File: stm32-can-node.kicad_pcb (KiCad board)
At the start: 4 copper layers, 40 x 25 mm, 41 parts, among them J1 Conn_01x04_Pin, J2 Conn_01x10_Pin, J3 Conn_01x10_Pin, J4 Conn_01x05_Pin, U1 DS2484R_T, U2 R-783.3-0.5, U3 STM32U535CETx, U4 SN65HVD234, Y1 16MHz

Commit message: better pcb layout
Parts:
- added C16: 100n, Capacitor_SMD:C_0402_1005Metric, F.Cu at (91.2, 53.5)
- moved C15 2.16 mm to (78.9, 63.7)
- moved C3 1.68 mm to (79.6, 65.2), turned to 0 degrees
- moved C6 1.56 mm to (76.1, 64.8), turned to -90 degrees
- moved R2 1.30 mm to (67.8, 54.5)
- moved C7 1.30 mm to (69.4, 54.1), turned to 0 degrees
- moved C14 0.58 mm to (78.4, 60.4)
- moved R6 0.35 mm to (86.4, 51.4)
- moved U1 0.30 mm to (88.6, 53.5)
- moved C4 0.26 mm to (66.4, 57.1), turned to -90 degrees
- moved C1 0.25 mm to (97.6, 65.7), turned to 0 degrees
- moved C2 0.20 mm to (84.5, 64.8), turned to 180 degrees
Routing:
- net +3.3V: track 22.8 -> 33.5 mm, vias 14 -> 15
- net CANH: track 20.3 -> 16.4 mm, vias 1 -> 2
- net CANL: track 20.2 -> 16.6 mm, vias 1 -> 2
- net Net-(U3-VCAP): track 3.47 -> 5.52 mm
- net GND: track 34.7 -> 36.5 mm, vias 25 -> 24
- net CAN_RX: track 4.86 -> 6.55 mm
- net +VIN: track 9.15 -> 7.85 mm
- net BOOT0: track 6.56 -> 5.74 mm, vias 2 -> 0

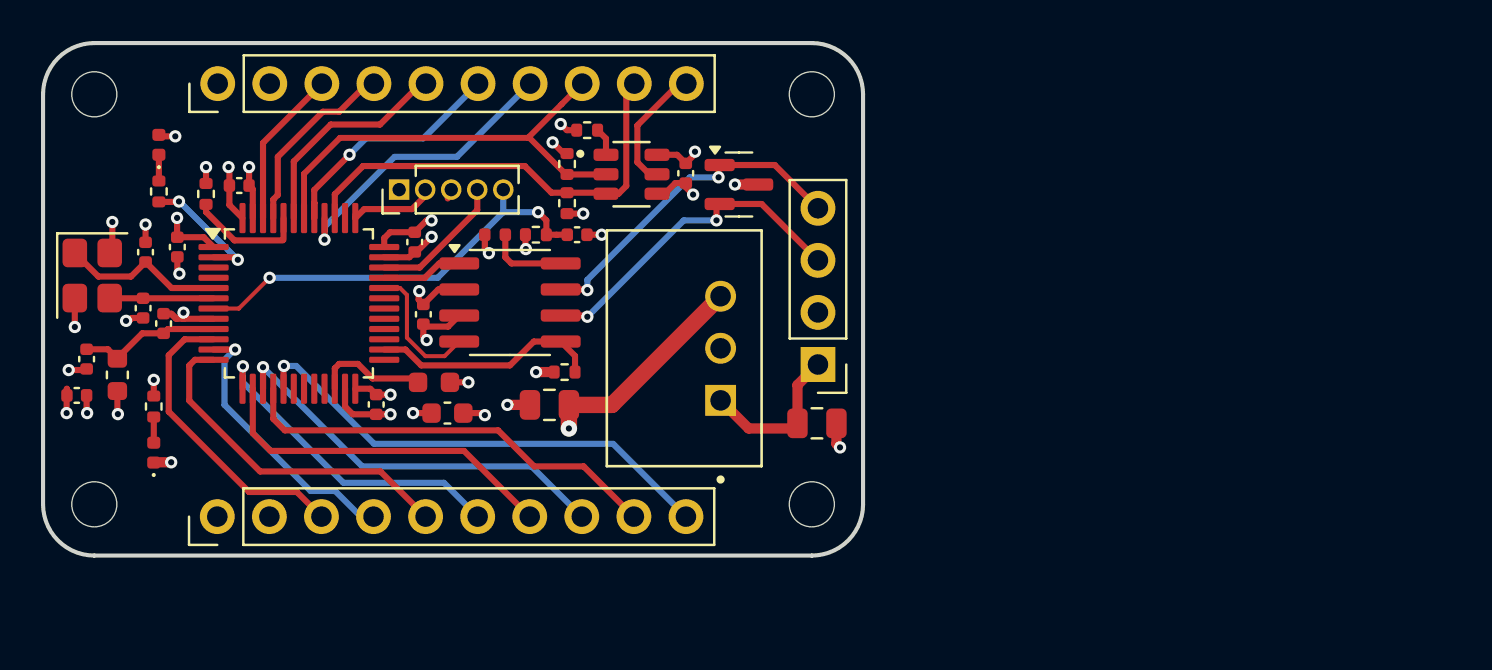
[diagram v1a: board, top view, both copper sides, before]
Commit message: change to 11-pin connectors
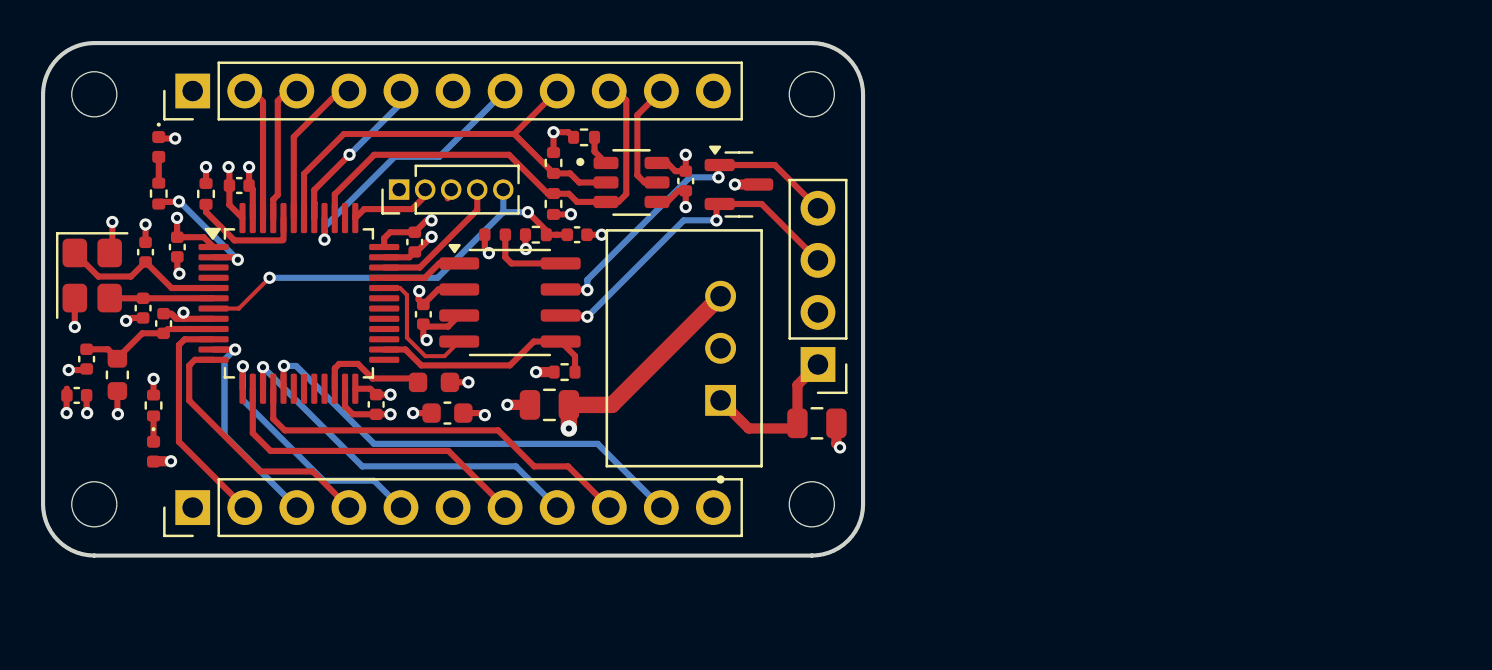
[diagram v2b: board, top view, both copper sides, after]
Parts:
- J2, J3: value Conn_01x10_Pin -> Conn_01x11_Pin; footprint Connector_PinHeader_2.54mm:PinHeader_1x10_P2.54mm_Vertical -> Connector_PinHeader_2.54mm:PinHeader_1x11_P2.54mm_Vertical
- moved J2 1.28 mm to (67.2, 69.8)
- moved J3 1.27 mm to (67.2, 49.5)
- moved R5 0.66 mm to (84.8, 53.0)
- moved R4 0.66 mm to (84.8, 55.0)
- moved U1 0.40 mm to (88.6, 54.0)
- moved R6 0.38 mm to (86.2, 51.8)
- moved C16 0.38 mm to (91.2, 53.9)
- moved D2 0.11 mm to (65.5, 52.2), turned to -90 degrees
- moved R9 0.11 mm to (65.5, 54.5)
- turned D1 to -90 degrees
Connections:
- D1 pad 1: +3.3V -> /PWR_LED_K
- D1 pad 2: /PWR_LED_K -> +3.3V
- D2 pad 1: Net-(D2-K) -> GND
- D2 pad 2: GND -> Net-(D2-A)
- J2 pad 2: GND -> PA0
- J2 pad 3: PA0 -> PA1
- J2 pad 4: PA1 -> PA2
- J2 pad 5: PA2 -> PA3
- J2 pad 6: PA3 -> GND
- J3 pad 2: GND -> PB9
- J3 pad 3: PB9 -> PB8
- J3 pad 4: PB8 -> PB7
- J3 pad 5: PB7 -> PB5
- J3 pad 6: PB5 -> GND
- R9 pad 2: Net-(D2-K) -> Net-(D2-A)
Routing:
- net PA2: track 16.9 -> 13.0 mm
- net PA0: track 14.8 -> 11.1 mm
- net PA3: track 16.1 -> 12.7 mm
- net PB7: track 11.0 -> 7.71 mm
- net PA1: track 13.5 -> 10.5 mm
- net PB8: track 9.25 -> 7.07 mm
- net PB4: track 14.6 -> 13.2 mm
- net PA6: track 21.0 -> 19.7 mm
- net PA5: track 19.6 -> 18.3 mm
- net PA4: track 17.4 -> 16.0 mm
- net PA7: track 23.8 -> 22.4 mm
- net Net-(D2-A): track 0.00 -> 1.28 mm
- net Net-(D2-K): track 1.28 -> 0.00 mm
- net I2C_SCL: track 22.2 -> 23.4 mm
- net PB9: track 8.05 -> 6.99 mm
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
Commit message: add step-down converter, update part values
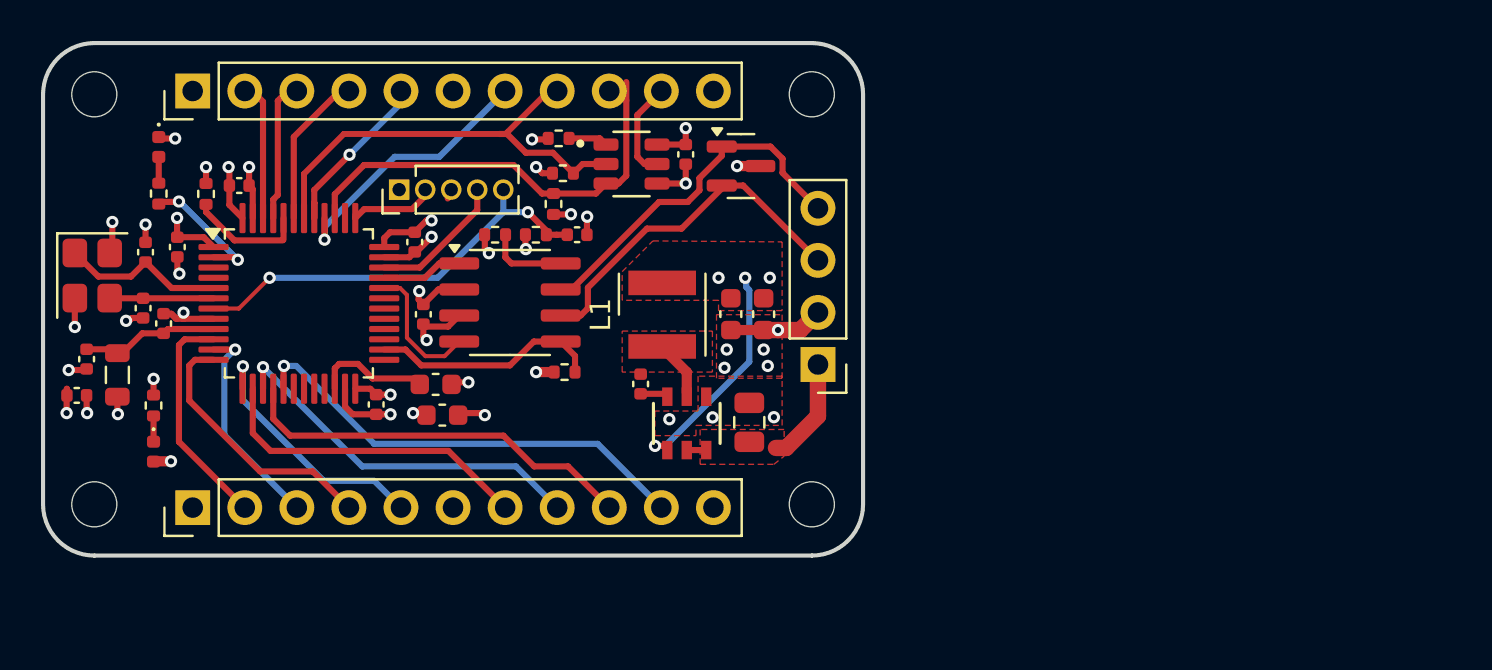
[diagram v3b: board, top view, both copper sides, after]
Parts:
- removed C2: 22u, Capacitor_SMD:C_0805_2012Metric
- removed U2: R-783.3-0.5, mrk:CONV_R-783.3-0.5
- added C18: 22uF, Capacitor_SMD:C_0603_1608Metric, F.Cu at (95.0, 60.4)
- added C19: 22uF, Capacitor_SMD:C_0603_1608Metric, F.Cu at (93.4, 60.4)
- added C20: 100nF, Capacitor_SMD:C_0402_1005Metric, F.Cu at (89.0, 63.8)
- added L1: 4.7uH, Inductor_SMD_Wurth:L_Wurth_WE-LQSH-4020, F.Cu at (90.0, 60.4)
- added U5: AP63203WU-7, footprints:AP63203WU-7_DIO, F.Cu at (91.2, 65.7)
- C1: value 22u -> 22uF
- C10, C11, C14, C16, C4, C5, C6, C7: value 100n -> 100nF
- C12, C13: value 10p -> 10pF
- C15: footprint PCM_JLCPCB:C_0603 -> Capacitor_SMD:C_0603_1608Metric
- C3: value 10u -> 10uF
- C8: value 10n -> 10nF
- C9: value 1u -> 1uF
- FB1: footprint Inductor_SMD:L_0603_1608Metric -> Inductor_SMD:L_0805_2012Metric
- R3: footprint PCM_JLCPCB:R_0402 -> Resistor_SMD:R_0402_1005Metric
- moved C1 3.30 mm to (94.3, 65.7), turned to 90 degrees
- moved C16 1.30 mm to (91.2, 52.6)
- moved R6 1.24 mm to (85.0, 51.8)
- moved D3 0.91 mm to (93.9, 53.1)
- moved U1 0.90 mm to (88.6, 53.1)
- moved R5 0.68 mm to (85.2, 53.5), turned to 0 degrees
- moved C3 0.27 mm to (79.3, 65.3)
- moved C15 0.13 mm to (79.0, 63.8)
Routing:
- net /SW: track 0.00 -> 3.05 mm
- net GND: track 35.9 -> 38.2 mm, vias 24 -> 30
- net +VIN: track 7.85 -> 6.16 mm
- net /BST: track 0.00 -> 1.45 mm
- net CANL: track 16.6 -> 17.8 mm, vias 2 -> 0
- net CANH: track 16.4 -> 17.4 mm, vias 2 -> 0
- net 1-W: track 5.70 -> 4.80 mm
- net I2C_SCL: track 23.4 -> 22.7 mm
- net +3.3V: track 33.8 -> 34.1 mm, vias 14 -> 18
- added copper zone on F.Cu, net +3.3V
- added copper zone on F.Cu, net +VIN
- added copper zone on F.Cu, net /SW
- added copper zone on F.Cu, net GND

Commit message: remove vias under mcu
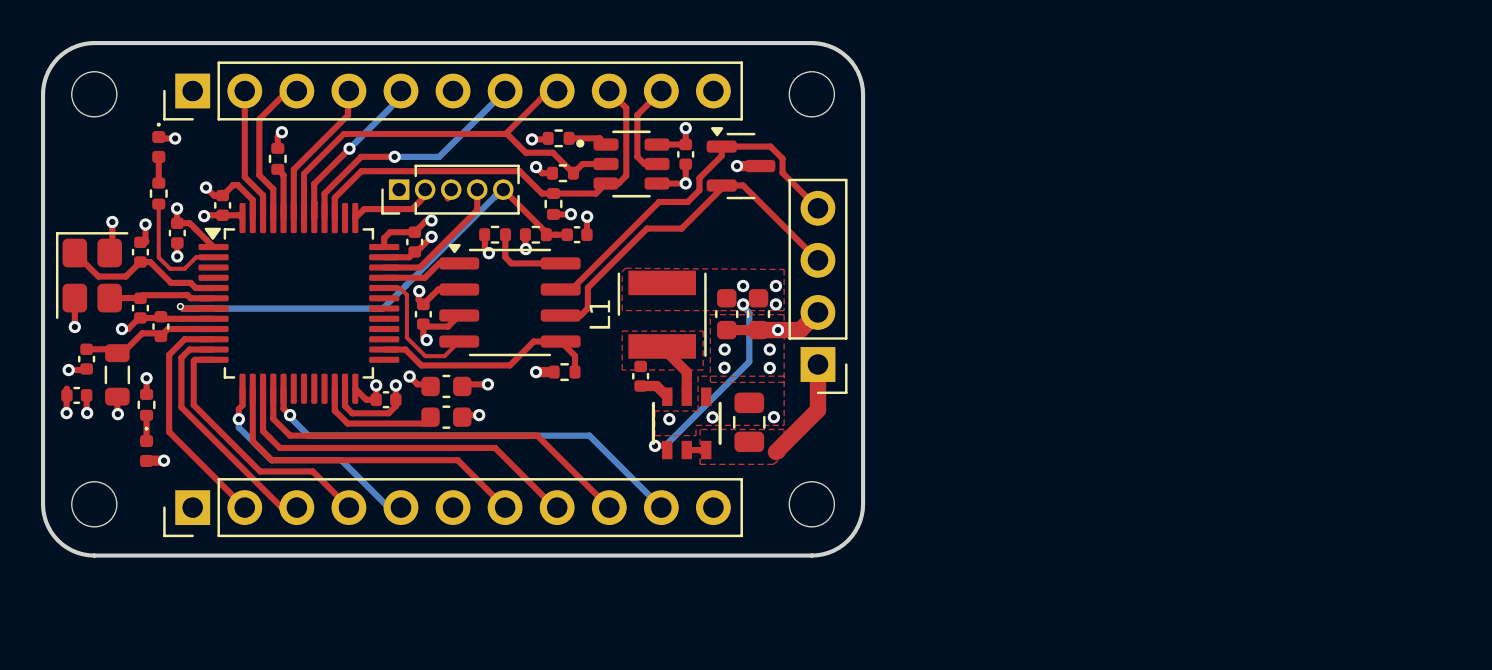
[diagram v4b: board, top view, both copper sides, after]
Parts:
- moved R2 3.90 mm to (71.3, 52.8)
- moved C15 1.68 mm to (79.5, 65.4)
- moved C3 1.41 mm to (79.5, 63.9)
- moved C7 1.26 mm to (68.6, 55.1), turned to 90 degrees
- moved C4 0.68 mm to (66.4, 56.4)
- moved C6 0.53 mm to (76.6, 64.5), turned to 0 degrees
- moved C20 0.38 mm to (89.0, 63.4)
- moved D1 0.34 mm to (64.9, 67.0)
- moved R1 0.34 mm to (64.9, 64.8)
- moved C12 0.25 mm to (64.6, 57.4)
- moved C18 0.25 mm to (94.8, 60.4)
- moved C19 0.20 mm to (93.2, 60.4)
- moved C8 0.20 mm to (65.6, 61.0)
- moved C13 0.13 mm to (64.6, 60.1)
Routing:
- net PB5: track 13.2 -> 9.45 mm
- net NRST: track 20.9 -> 24.1 mm, vias 2 -> 1
- net BOOT0: track 5.74 -> 2.49 mm
- net GND: track 38.2 -> 41.4 mm, vias 30 -> 29
- net I2C_SCL: track 22.7 -> 21.0 mm
- net PA1: track 10.5 -> 11.8 mm, vias 1 -> 0
- net PA3: track 12.7 -> 11.5 mm
- net +3.3V: track 34.1 -> 32.9 mm, vias 18 -> 19
- net PB4: track 13.2 -> 12.1 mm
- net PA7: track 22.4 -> 21.5 mm
- net Net-(U3-VCAP): track 5.52 -> 6.40 mm
- net PB8: track 7.07 -> 7.63 mm
- net USER LED: track 6.27 -> 5.74 mm, vias 2 -> 0
- net PA5: track 18.3 -> 18.0 mm, vias 1 -> 0

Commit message: support for UFQFPN48_SMPS
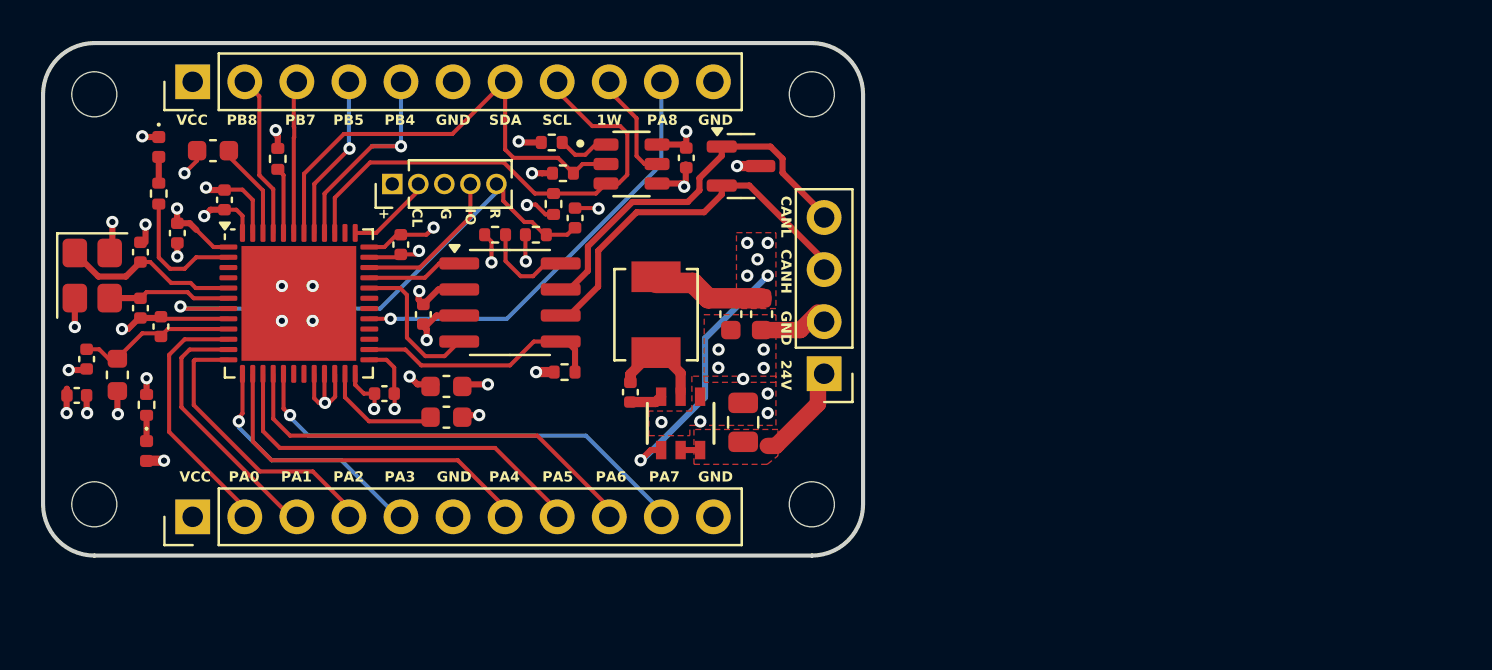
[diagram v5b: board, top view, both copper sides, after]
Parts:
- removed U3: STM32U535CETx, Package_QFP:LQFP-48_7x7mm_P0.5mm
- added C30: 2.2uF, Capacitor_SMD:C_0603_1608Metric, F.Cu at (68.1, 52.4)
- added G***: LOGO, mrk:robbo2, F.Cu at (86.6, 66.6)
- added U3_1: STM32U535CEUxQ, Package_DFN_QFN:QFN-48-1EP_7x7mm_P0.5mm_EP5.6x5.6mm, F.Cu at (72.3, 59.9)
- C15: value 4.7uF -> 2.2uF
- D1: value RED -> C397045
- D2: value RED -> C165977
- FB1: value 120R -> FCM1608KF-601T05; footprint Inductor_SMD:L_0805_2012Metric -> Inductor_SMD:L_0603_1608Metric
- L1: footprint Inductor_SMD_Wurth:L_Wurth_WE-LQSH-4020 -> mrk:IND_SRP4020TA-4R7M
- R1, R4, R5, R6, R9: value 1k5 -> 1.5kΩ
- R2, R7, R8: value 10k -> 10kΩ
- R3: value 0 -> 0Ω
- U1: value DS2484R_T -> DS2484R+T
- U4: value SN65HVD234 -> SN65HVD234DR
- moved C20 0.93 mm to (88.5, 64.2)
- moved C11 0.83 mm to (85.8, 55.7), turned to -90 degrees
- moved C5 0.69 mm to (77.3, 57.0)
- moved J1 0.54 mm to (98.0, 63.3)
- moved J2 0.45 mm to (67.2, 70.3)
- moved J3 0.45 mm to (67.2, 49.0)
- moved J4 0.43 mm to (76.9, 54.0)
- moved R6 0.39 mm to (84.7, 52.0)
- moved C6 0.31 mm to (76.5, 64.2), turned to 180 degrees
- moved C1 0.30 mm to (94.0, 65.7)
- moved L1 0.30 mm to (89.8, 60.4)
- moved U5 0.30 mm to (90.9, 65.7)
- moved C7 0.28 mm to (68.7, 54.8)
- moved C19 0.20 mm to (93.4, 60.4)
- moved C16 0.17 mm to (91.2, 52.8)
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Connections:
- J3 pad 10: 1-W -> PA8
- J3 pad 2: PB9 -> PB8
- J3 pad 3: PB8 -> PB7
- J3 pad 4: PB7 -> PB5
- J3 pad 5: PB5 -> PB4
- J3 pad 7: PB4 -> I2C_SDA
- J3 pad 8: I2C_SDA -> I2C_SCL
- J3 pad 9: I2C_SCL -> 1-W
- R3 pad 1: GND -> /CAN_RS
- R3 pad 2: /CAN_RS -> GND
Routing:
- net PA8: track 0.00 -> 20.9 mm, vias 0 -> 1
- net +3.3V: track 32.9 -> 46.0 mm, vias 19 -> 20
- net PB9: track 6.57 -> 0.00 mm
- net Net-(C30-Pad1): track 0.00 -> 4.42 mm
- net I2C_SCL: track 21.0 -> 24.0 mm
- net GND: track 41.4 -> 44.1 mm, vias 29 -> 36
- net /SW: track 3.05 -> 5.19 mm
- net I2C_SDA: track 22.0 -> 23.5 mm
- net PB5: track 9.45 -> 8.10 mm
- net NRST: track 24.1 -> 25.2 mm
- net PB7: track 7.71 -> 6.79 mm
- net SWDIO: track 6.70 -> 7.56 mm
- net Net-(C15-Pad1): track 6.40 -> 5.60 mm
- net PA7: track 21.5 -> 22.3 mm
- net CAN_RX: track 6.55 -> 7.28 mm
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- removed copper zone on F.Cu, net /SW
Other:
- board text added: "+"
- board text added: "1W"
- board text added: "CAN Board v1"
- board text added: "CL"
- board text added: "G"
- board text added: "IO"
- board text added: "PA0"
- board text added: "PA1"
- board text added: "PA2"
- board text added: "PA3"
- board text added: "PA4"
- board text added: "PA5"
- board text added: "PA6"
- board text added: "PA7"
- board text added: "PA8"
- board text added: "PB4"
- board text added: "PB5"
- board text added: "PB7"
- board text added: "PB8"
- board text added: "R"
- board text added: "SCL"
- board text added: "SDA"
- board text added: "VCC"
- board text added: "mrk 2025"

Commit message: update images
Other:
- board text added: "C"
- board text added: "SWD"
- board text added: "V"
- board text removed: "+"
- board text removed: "CL"
